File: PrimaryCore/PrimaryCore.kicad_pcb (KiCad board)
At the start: 2 copper layers, 94 x 76.2 mm, 11 parts, among them J1 Screw_Terminal_01x02, J2 Screw_Terminal_01x06, J3 Screw_Terminal_01x02, Q1 Q_NMOS_DGS, Q2 Q_NMOS_DGS, Q3 Q_NMOS_DGS, Q4 Q_NMOS_DGS

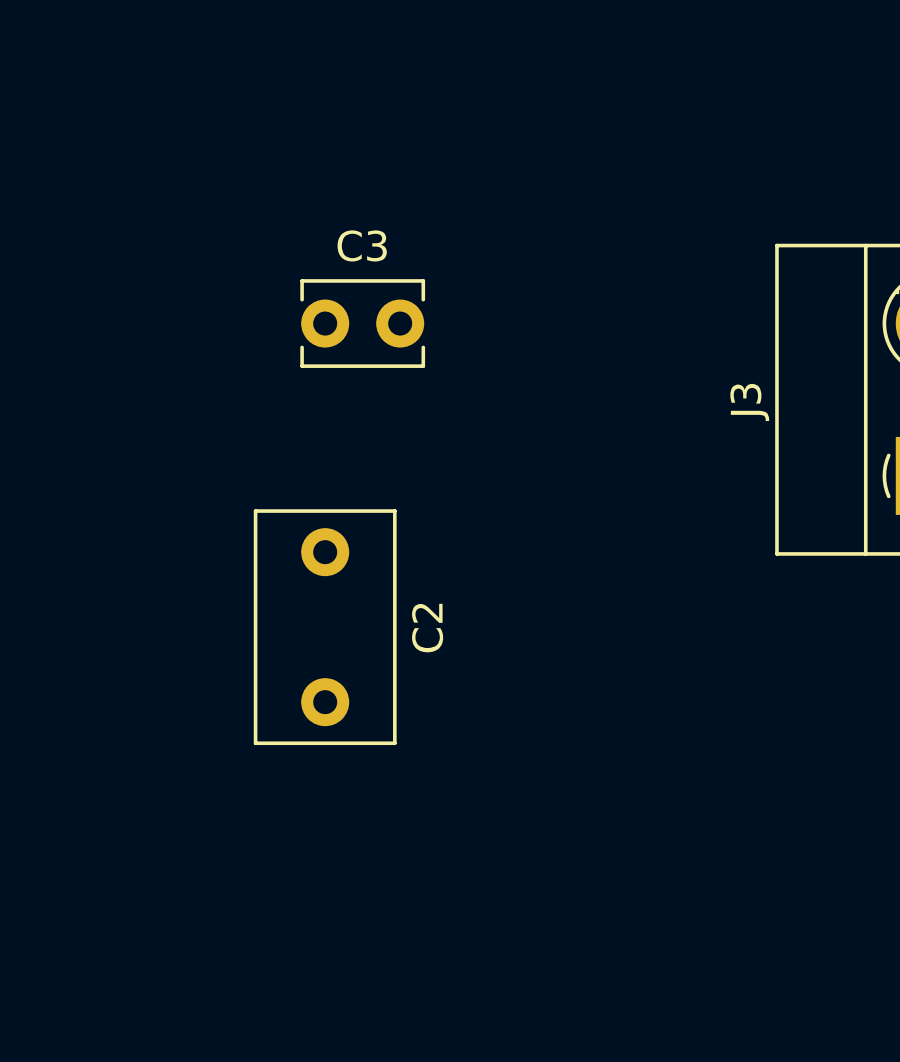
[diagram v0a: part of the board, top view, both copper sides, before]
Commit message: Change Cap footpackage p 10mm
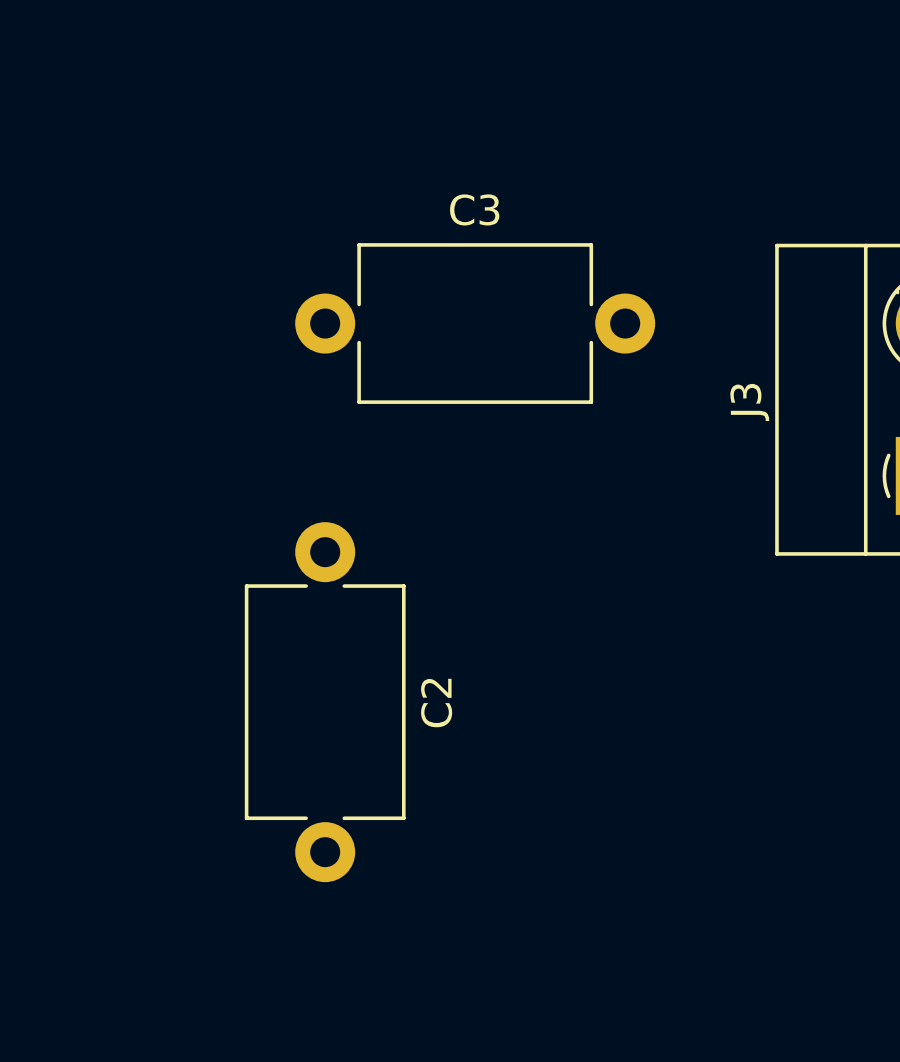
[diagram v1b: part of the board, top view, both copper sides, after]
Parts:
- C2: footprint Capacitor_THT:C_Disc_D7.5mm_W4.4mm_P5.00mm -> Capacitor_THT:C_Disc_D7.5mm_W5.0mm_P10.00mm
- C3: footprint Capacitor_THT:C_Disc_D3.8mm_W2.6mm_P2.50mm -> Capacitor_THT:C_Disc_D7.5mm_W5.0mm_P10.00mm
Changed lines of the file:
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@@
     )
   )
-  (footprint "Capacitor_THT:C_Disc_D3.8mm_W2.6mm_P2.50mm" (layer "F.Cu")
+  (footprint "Capacitor_THT:C_Disc_D7.5mm_W5.0mm_P10.00mm" (layer "F.Cu")
     (at 182.88 76.2)
-    (descr "C, Disc series, Radial, pin pitch=2.50mm, , diameter*width=3.8*2.6mm^2, Capacitor, http://www.vishay.com/docs/45233/krseries.pdf")
-    (tags "C Disc series Radial pin pitch 2.50mm  diameter 3.8mm width 2.6mm Capacitor")
+    (descr "C, Disc series, Radial, pin pitch=10.00mm, , diameter*width=7.5*5.0mm^2, Capacitor, http://www.vishay.com/docs/28535/vy2series.pdf")
+    (tags "C Disc series Radial pin pitch 10.00mm  diameter 7.5mm width 5.0mm Capacitor")
     (property "Sheetfile" "PrimaryCore.kicad_sch")
     (property "Sheetname" "")
     (attr through_hole)
-    (fp_text reference "C3" (at 1.25 -2.55) (layer "F.SilkS")
+    (fp_text reference "C3" (at 5 -3.75) (layer "F.SilkS")
       (effects (font (size 1 1) (thickness 0.15)))
     )
-    (fp_text value "270pF" (at 1.25 2.55) (layer "F.Fab")
+    (fp_text value "270pF" (at 5 3.75) (layer "F.Fab")
       (effects (font (size 1 1) (thickness 0.15)))
     )
-    (fp_text user "${REFERENCE}" (at 1.25 0) (layer "F.Fab")
-      (effects (font (size 0.76 0.76) (thickness 0.114)))
+    (fp_text user "${REFERENCE}" (at 5 0) (layer "F.Fab")
+      (effects (font (size 1 1) (thickness 0.15)))
     )
-    (fp_line (start -0.77 1.42) (end 3.27 1.42) (layer "F.SilkS") (width 0.12))
-    (fp_line (start -0.77 -1.42) (end 3.27 -1.42) (layer "F.SilkS") (width 0.12))
-    (fp_line (start -0.77 0.795) (end -0.77 1.42) (layer "F.SilkS") (width 0.12))
-    (fp_line (start -0.77 -1.42) (end -0.77 -0.795) (layer "F.SilkS") (width 0.12))
-    (fp_line (start 3.27 -1.42) (end 3.27 -0.795) (layer "F.SilkS") (width 0.12))
-    (fp_line (start 3.27 0.795) (end 3.27 1.42) (layer "F.SilkS") (width 0.12))
-    (fp_line (start -1.05 1.55) (end 3.55 1.55) (layer "F.CrtYd") (width 0.05))
-    (fp_line (start 3.55 1.55) (end 3.55 -1.55) (layer "F.CrtYd") (width 0.05))
-    (fp_line (start -1.05 -1.55) (end -1.05 1.55) (layer "F.CrtYd") (width 0.05))
-    (fp_line (start 3.55 -1.55) (end -1.05 -1.55) (layer "F.CrtYd") (width 0.05))
-    (fp_line (start 3.15 -1.3) (end -0.65 -1.3) (layer "F.Fab") (width 0.1))
-    (fp_line (start -0.65 -1.3) (end -0.65 1.3) (layer "F.Fab") (width 0.1))
-    (fp_line (start 3.15 1.3) (end 3.15 -1.3) (layer "F.Fab") (width 0.1))
-    (fp_line (start -0.65 1.3) (end 3.15 1.3) (layer "F.Fab") (width 0.1))
-    (pad "1" thru_hole circle (at 0 0) (size 1.6 1.6) (drill 0.8) (layers *.Cu *.Mask)
+    (fp_line (start 1.13 2.62) (end 8.87 2.62) (layer "F.SilkS") (width 0.12))
+    (fp_line (start 8.87 -2.62) (end 8.87 -0.636) (layer "F.SilkS") (width 0.12))
+    (fp_line (start 1.13 -2.62) (end 1.13 -0.636) (layer "F.SilkS") (width 0.12))
+    (fp_line (start 1.13 0.636) (end 1.13 2.62) (layer "F.SilkS") (width 0.12))
+    (fp_line (start 8.87 0.636) (end 8.87 2.62) (layer "F.SilkS") (width 0.12))
+    (fp_line (start 1.13 -2.62) (end 8.87 -2.62) (layer "F.SilkS") (width 0.12))
+    (fp_line (start -1.25 2.75) (end 11.25 2.75) (layer "F.CrtYd") (width 0.05))
+    (fp_line (start 11.25 2.75) (end 11.25 -2.75) (layer "F.CrtYd") (width 0.05))
+    (fp_line (start 11.25 -2.75) (end -1.25 -2.75) (layer "F.CrtYd") (width 0.05))
+    (fp_line (start -1.25 -2.75) (end -1.25 2.75) (layer "F.CrtYd") (width 0.05))
+    (fp_line (start 1.25 2.5) (end 8.75 2.5) (layer "F.Fab") (width 0.1))
+    (fp_line (start 8.75 2.5) (end 8.75 -2.5) (layer "F.Fab") (width 0.1))
+    (fp_line (start 8.75 -2.5) (end 1.25 -2.5) (layer "F.Fab") (width 0.1))
+    (fp_line (start 1.25 -2.5) (end 1.25 2.5) (layer "F.Fab") (width 0.1))
+    (pad "1" thru_hole circle (at 0 0) (size 2 2) (drill 1) (layers *.Cu *.Mask)
       (net 3 "Net-(C2-Pad1)") (pintype "passive"))
-    (pad "2" thru_hole circle (at 2.5 0) (size 1.6 1.6) (drill 0.8) (layers *.Cu *.Mask)
+    (pad "2" thru_hole circle (at 10 0) (size 2 2) (drill 1) (layers *.Cu *.Mask)
       (net 5 "Net-(C3-Pad2)") (pintype "passive"))
-    (model "${KICAD6_3DMODEL_DIR}/Capacitor_THT.3dshapes/C_Disc_D3.8mm_W2.6mm_P2.50mm.wrl"
+    (model "${KICAD6_3DMODEL_DIR}/Capacitor_THT.3dshapes/C_Disc_D7.5mm_W5.0mm_P10.00mm.wrl"
       (offset (xyz 0 0 0))
       (scale (xyz 1 1 1))
@@
     )
   )
-  (footprint "Capacitor_THT:C_Disc_D7.5mm_W4.4mm_P5.00mm" (layer "F.Cu")
+  (footprint "Capacitor_THT:C_Disc_D7.5mm_W5.0mm_P10.00mm" (layer "F.Cu")
     (at 182.88 83.82 -90)
-    (descr "C, Disc series, Radial, pin pitch=5.00mm, , diameter*width=7.5*4.4mm^2, Capacitor")
-    (tags "C Disc series Radial pin pitch 5.00mm  diameter 7.5mm width 4.4mm Capacitor")
+    (descr "C, Disc series, Radial, pin pitch=10.00mm, , diameter*width=7.5*5.0mm^2, Capacitor, http://www.vishay.com/docs/28535/vy2series.pdf")
+    (tags "C Disc series Radial pin pitch 10.00mm  diameter 7.5mm width 5.0mm Capacitor")
     (property "Sheetfile" "PrimaryCore.kicad_sch")
     (property "Sheetname" "")
     (attr through_hole)
-    (fp_text reference "C2" (at 2.5 -3.45 90) (layer "F.SilkS")
+    (fp_text reference "C2" (at 5 -3.75 -90) (layer "F.SilkS")
       (effects (font (size 1 1) (thickness 0.15)))
     )
-    (fp_text value "330pF" (at 2.5 3.45 90) (layer "F.Fab")
+    (fp_text value "330pF" (at 5 3.75 -90) (layer "F.Fab")
       (effects (font (size 1 1) (thickness 0.15)))
     )
-    (fp_text user "${REFERENCE}" (at 2.5 0 90) (layer "F.Fab")
+    (fp_text user "${REFERENCE}" (at 5 0 -90) (layer "F.Fab")
       (effects (font (size 1 1) (thickness 0.15)))
     )
-    (fp_line (start 6.37 -2.321) (end 6.37 2.321) (layer "F.SilkS") (width 0.12))
-    (fp_line (start -1.37 2.321) (end 6.37 2.321) (layer "F.SilkS") (width 0.12))
-    (fp_line (start -1.37 -2.321) (end -1.37 2.321) (layer "F.SilkS") (width 0.12))
-    (fp_line (start -1.37 -2.321) (end 6.37 -2.321) (layer "F.SilkS") (width 0.12))
-    (fp_line (start -1.5 2.45) (end 6.5 2.45) (layer "F.CrtYd") (width 0.05))
-    (fp_line (start -1.5 -2.45) (end -1.5 2.45) (layer "F.CrtYd") (width 0.05))
-    (fp_line (start 6.5 -2.45) (end -1.5 -2.45) (layer "F.CrtYd") (width 0.05))
-    (fp_line (start 6.5 2.45) (end 6.5 -2.45) (layer "F.CrtYd") (width 0.05))
-    (fp_line (start -1.25 2.2) (end 6.25 2.2) (layer "F.Fab") (width 0.1))
-    (fp_line (start 6.25 2.2) (end 6.25 -2.2) (layer "F.Fab") (width 0.1))
-    (fp_line (start -1.25 -2.2) (end -1.25 2.2) (layer "F.Fab") (width 0.1))
-    (fp_line (start 6.25 -2.2) (end -1.25 -2.2) (layer "F.Fab") (width 0.1))
-    (pad "1" thru_hole circle (at 0 0 270) (size 1.6 1.6) (drill 0.8) (layers *.Cu *.Mask)
+    (fp_line (start 1.13 2.62) (end 8.87 2.62) (layer "F.SilkS") (width 0.12))
+    (fp_line (start 8.87 0.636) (end 8.87 2.62) (layer "F.SilkS") (width 0.12))
+    (fp_line (start 1.13 -2.62) (end 8.87 -2.62) (layer "F.SilkS") (width 0.12))
+    (fp_line (start 1.13 -2.62) (end 1.13 -0.636) (layer "F.SilkS") (width 0.12))
+    (fp_line (start 1.13 0.636) (end 1.13 2.62) (layer "F.SilkS") (width 0.12))
+    (fp_line (start 8.87 -2.62) (end 8.87 -0.636) (layer "F.SilkS") (width 0.12))
+    (fp_line (start 11.25 -2.75) (end -1.25 -2.75) (layer "F.CrtYd") (width 0.05))
+    (fp_line (start -1.25 -2.75) (end -1.25 2.75) (layer "F.CrtYd") (width 0.05))
+    (fp_line (start -1.25 2.75) (end 11.25 2.75) (layer "F.CrtYd") (width 0.05))
+    (fp_line (start 11.25 2.75) (end 11.25 -2.75) (layer "F.CrtYd") (width 0.05))
+    (fp_line (start 1.25 2.5) (end 8.75 2.5) (layer "F.Fab") (width 0.1))
+    (fp_line (start 8.75 2.5) (end 8.75 -2.5) (layer "F.Fab") (width 0.1))
+    (fp_line (start 1.25 -2.5) (end 1.25 2.5) (layer "F.Fab") (width 0.1))
+    (fp_line (start 8.75 -2.5) (end 1.25 -2.5) (layer "F.Fab") (width 0.1))
+    (pad "1" thru_hole circle (at 0 0 270) (size 2 2) (drill 1) (layers *.Cu *.Mask)
       (net 3 "Net-(C2-Pad1)") (pintype "passive"))
-    (pad "2" thru_hole circle (at 5 0 270) (size 1.6 1.6) (drill 0.8) (layers *.Cu *.Mask)
+    (pad "2" thru_hole circle (at 10 0 270) (size 2 2) (drill 1) (layers *.Cu *.Mask)
       (net 4 "Net-(C2-Pad2)") (pintype "passive"))
-    (model "${KICAD6_3DMODEL_DIR}/Capacitor_THT.3dshapes/C_Disc_D7.5mm_W4.4mm_P5.00mm.wrl"
+    (model "${KICAD6_3DMODEL_DIR}/Capacitor_THT.3dshapes/C_Disc_D7.5mm_W5.0mm_P10.00mm.wrl"
       (offset (xyz 0 0 0))
       (scale (xyz 1 1 1))

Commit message: latest route pcb
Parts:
- C1: footprint TerminalBlock_Phoenix:TerminalBlock_Phoenix_MPT-0,5-2-2.54_1x02_P2.54mm_Horizontal -> Capacitor_THT:CP_Radial_D18.0mm_P7.50mm
- moved Q2 62.2 mm to (165.3, 47.9), turned to -90 degrees
- moved Q3 52.3 mm to (139.5, 104.5)
- moved J1 28.0 mm to (91.4, 74.9)
- moved C1 23.8 mm to (110.8, 74.0)
- moved Q1 10.9 mm to (139.9, 47.9), turned to -90 degrees
- moved J2 4.38 mm to (183.2, 113.6)
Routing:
- net /IN2: track 0.00 -> 250.5 mm
- net VDD: track 0.00 -> 231.9 mm, vias 0 -> 6
- net /IN1: track 0.00 -> 214.7 mm
- net Net-(C2-Pad2): track 0.00 -> 85.5 mm
- net /IN3: track 0.00 -> 62.0 mm
- net Net-(L1-Pad1): track 0.00 -> 48.8 mm
- net Net-(C2-Pad1): track 0.00 -> 43.4 mm
- net /IN4: track 0.00 -> 39.1 mm
- net Net-(C3-Pad2): track 0.00 -> 10.3 mm
- net GND: vias 0 -> 20
- added copper zone on B.Cu, net GND
- added copper zone on F.Cu, net GND
- added copper zone on F.Cu, net VDD
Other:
- board size 94 x 76.2 mm -> 121.9 x 85.1 mm
